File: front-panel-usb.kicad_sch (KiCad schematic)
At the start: 83 parts, among them J2 USB-C_Kycon_KUSBX-SL2-CS1N24-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, J3 USB-C_Kycon_KUSBX-SL2-CS1N24-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, J4 USB-C_Kycon_KUSBX-SL2-CS1N24-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, Q1 BSS84AKW, U10 TPD4E05U06QDQARQ1, U4 TPD4E05U06QDQARQ1, U5 FT4232H_VQFN, U6 NCP718BSN330T1G, U7 AP22615A_TSOT26, U8 AP22615A_TSOT26, U9 TPD4E05U06QDQARQ1, Y1 Resonator_12MHz_ABM8G

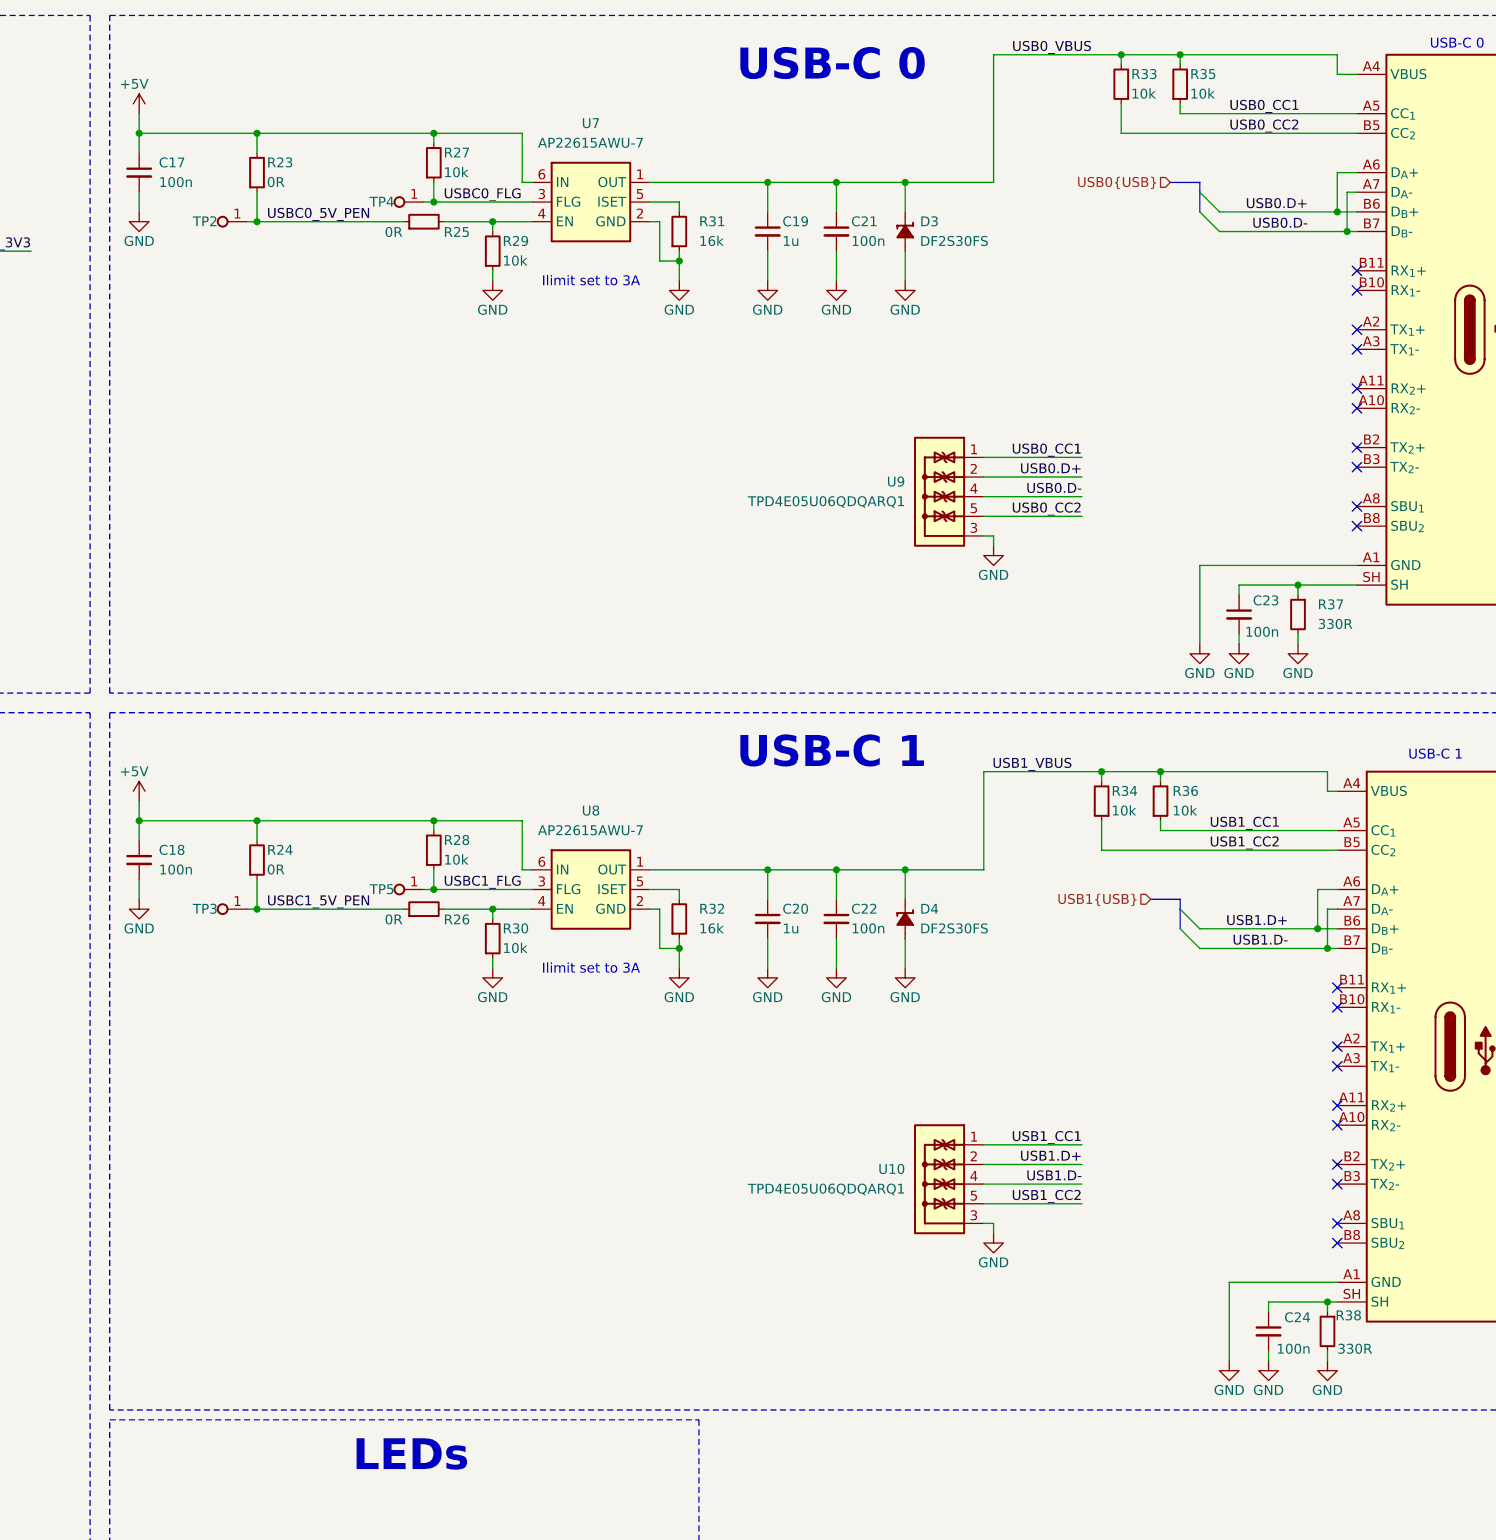
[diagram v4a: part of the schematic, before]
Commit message: Add CC controllers to USB0 and USB1
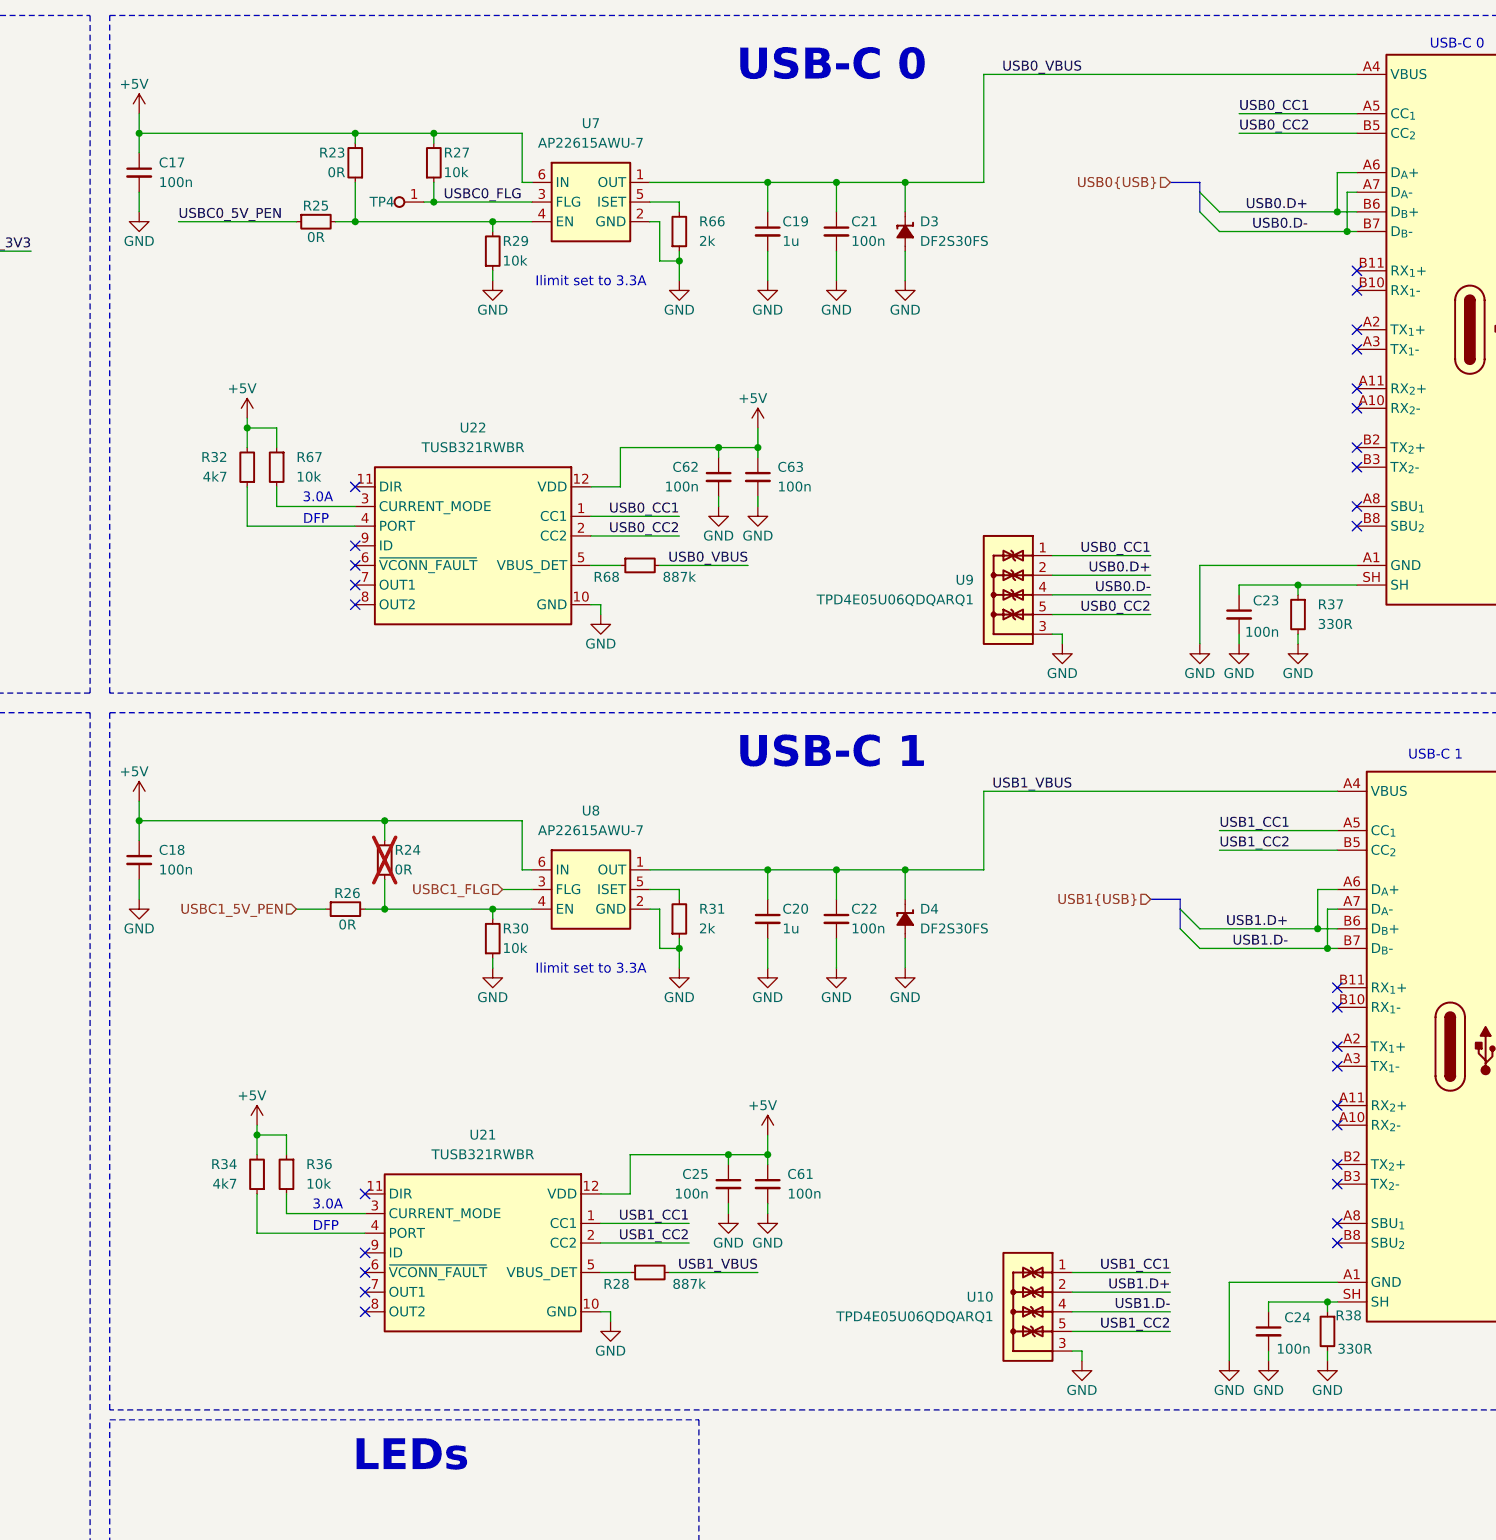
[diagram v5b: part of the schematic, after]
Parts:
- removed R28, R33, R34, R35, R36: R_10k_0402, antmicro-footprints:R_0402_1005Metric, symbol antmicroResistors0402:R_10k_0402
- removed R31, R32: R_16k_0402, antmicro-footprints:R_0402_1005Metric, symbol antmicroResistors0402:R_16k_0402
- removed TP2, TP3, TP5: TP_0.75mm_SMD, antmicro-footprints:TP_SMD_0.75mm, symbol antmicroTestPoints:TP_0.75mm_SMD
- added C25, C61, C62, C63: C_100n_0402, antmicro-footprints:C_0402_1005Metric, symbol antmicroCapacitors0402:C_100n_0402
- added R28, R68: R_887k_0402, antmicro-footprints:R_0402_1005Metric, symbol Resistors0402:R_887k_0402
- added R31, R66: R_2k_0402, antmicro-footprints:R_0402_1005Metric, symbol Resistors0402:R_2k_0402
- added R32, R34: R_4k7_0402, antmicro-footprints:R_0402_1005Metric, symbol Resistors0402:R_4k7_0402
- added R36, R67: R_10k_0402, antmicro-footprints:R_0402_1005Metric, symbol Resistors0402:R_10k_0402
- added U21, U22: TUSB321RWBR, antmicro-footprints:Texas_X2QFN-12_1.6x1.6mm_P0.4mm, symbol InterfaceControllers:TUSB321RWBR
- R24: now not fitted; now left out of the parts list
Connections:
- net +5V: now also C25.1, C61.1, C62.1, C63.1, R32.2, R34.2, R36.1, R67.1, U21.12 (VDD), U22.12 (VDD)
- net GND: now also C25.2, C61.2, C62.2, C63.2, R31.1, R66.1, U21.10 (GND), U22.10 (GND)
- net USB0_CC1: now also U22.1 (CC1)
- net USB0_CC2: now also U22.2 (CC2)
- net USB0_VBUS: now also R68.2
- net USB1_CC1: now also U21.1 (CC1)
- net USB1_CC2: now also U21.2 (CC2)
- net USB1_VBUS: now also R28.2
- net USBC0_5V_PEN: no longer R23.1
- net USBC1_5V_PEN: no longer R24.1
- net at U7.5 (ISET): now also R66.2
- net at R26.2, R30.2, U8.4 (EN): now also R24.1
- net at U8.5 (ISET): now also R31.2
- net at R25.2, R29.2, U7.4 (EN): now also R23.1
- new net: R36.2, U21.3 (CURRENT_MODE)
- new net: R67.2, U22.3 (CURRENT_MODE)
- new net: R68.1, U22.5 (VBUS_DET)
- new net: R32.1, U22.4 (PORT)
- new net: R28.1, U21.5 (VBUS_DET)
- new net: R34.1, U21.4 (PORT)
- no-connect marks 57 -> 67
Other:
- note added: "3.0A"
- note added: "DFP"
- note added: "Ilimit set to 3.3A"
- note removed: "Ilimit set to 3A"
- moved on the sheet: R23, R25, R26, U10, U9

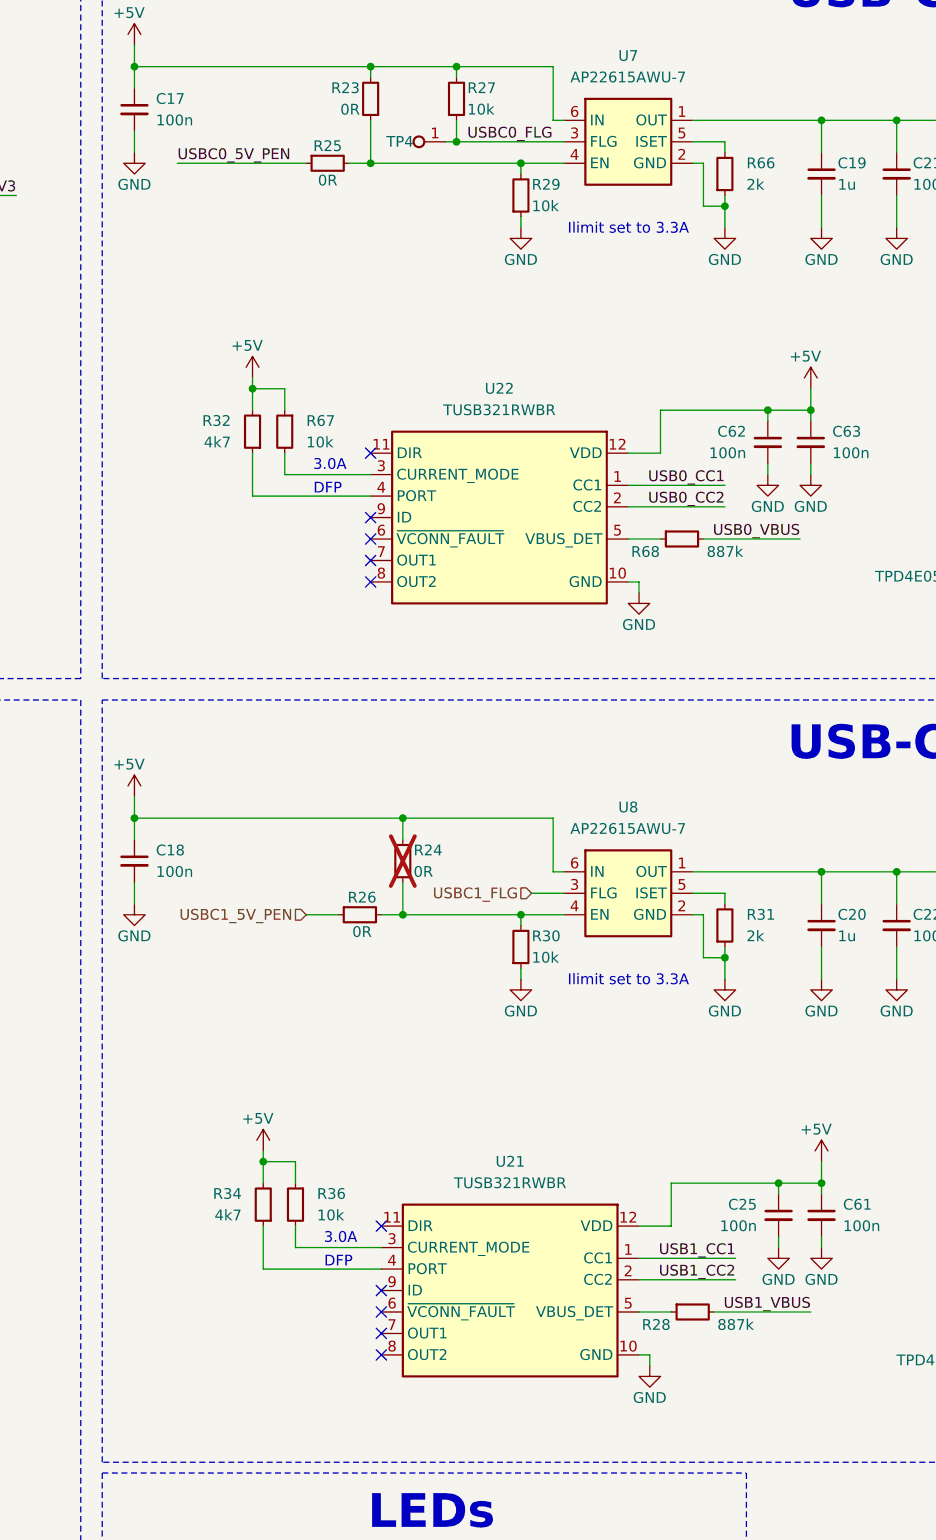
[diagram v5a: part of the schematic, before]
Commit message: Change USB0 and USB1 to advertise as 500mA source
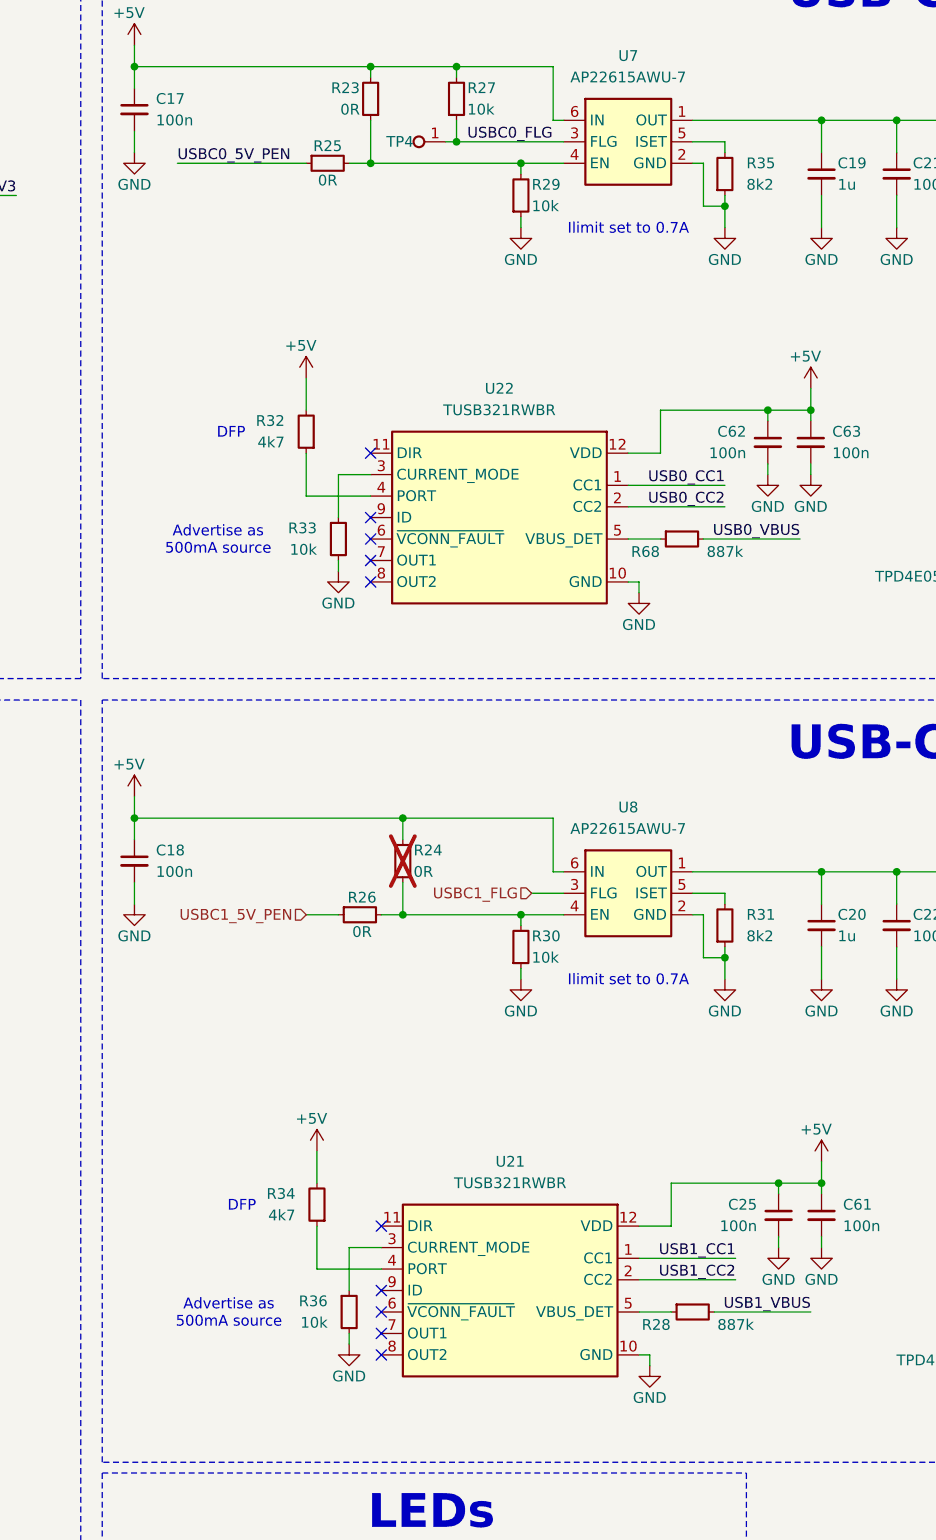
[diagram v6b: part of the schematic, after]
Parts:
- removed R31, R66: R_2k_0402, antmicro-footprints:R_0402_1005Metric, symbol Resistors0402:R_2k_0402
- removed R67: R_10k_0402, antmicro-footprints:R_0402_1005Metric, symbol Resistors0402:R_10k_0402
- added R31, R35: R_8k2_0402, antmicro-footprints:R_0402_1005Metric, symbol Resistors0402:R_8k2_0402
- added R33: R_10k_0402, antmicro-footprints:R_0402_1005Metric, symbol Resistors0402:R_10k_0402
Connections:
- net +5V: no longer R36.1
- net GND: now also R36.2, R31.1, R33.2, R35.1
- net at U21.3 (CURRENT_MODE): now also R36.1; no longer R36.2
- net at U22.3 (CURRENT_MODE): now also R33.1
- net at U7.5 (ISET): now also R35.2
- net at U8.5 (ISET): now also R31.2
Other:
- note added: "Advertise as 500mA source"
- note added: "Ilimit set to 0.7A"
- note removed: "3.0A"
- note removed: "Ilimit set to 3.3A"
- moved on the sheet: R34, R36
